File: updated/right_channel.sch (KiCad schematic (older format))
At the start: 20 parts, among them J4 Left 0 ohms, J5 Right 8 ohms, J6 Conn_Coaxial, T3 AudioTxfmr

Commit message: finish updated schematic
Convert tables from google doc to markdown to have these in this repo
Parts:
- removed RV1B: R_POT, symbol Device:R_POT
- removed V4,V5: 6P1, symbol local:6P1
- removed V7: 6H8C, symbol local:6H8C
- added RV1: R_POT_Dual_Separate, symbol Device:R_POT_Dual_Separate
- added V3: 12AX7, Valve:Valve_ECC-83-1, symbol local:12AX7
- added V4: EL84, Valve:Valve_ECC-83-1, symbol local:EL84
- C10, C11: footprint (none) -> Capacitor_THT:CP_Radial_D4.0mm_P2.00mm
- C12, C8: footprint (none) -> Capacitor_THT:CP_Radial_D10.0mm_P5.00mm
- C9: renamed from C12; footprint (none) -> Capacitor_THT:CP_Radial_D10.0mm_P5.00mm
- R10, R11, R7, R8, R9: footprint (none) -> Resistor_THT:R_Axial_DIN0516_L15.5mm_D5.0mm_P20.32mm_Horizontal
- R12: renamed from R?; footprint (none) -> Resistor_THT:R_Axial_DIN0516_L15.5mm_D5.0mm_P20.32mm_Horizontal
- R16: renamed from R16,17; footprint (none) -> Resistor_THT:R_Axial_DIN0516_L15.5mm_D5.0mm_P20.32mm_Horizontal
- R18: renamed from R13; footprint (none) -> Resistor_THT:R_Axial_DIN0516_L15.5mm_D5.0mm_P20.32mm_Horizontal
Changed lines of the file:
@@
 F 0 "C8" H 4318 1941 50  0000 L CNN
 F 1 "22uF" H 4318 1850 50  0000 L CNN
-F 2 "" H 4238 1700 50  0001 C CNN
+F 2 "Capacitor_THT:CP_Radial_D10.0mm_P5.00mm" H 4238 1700 50  0001 C CNN
 F 3 "~" H 4200 1850 50  0001 C CNN
 F 4 "450V" H 4318 1759 50  0000 L CNN "Voltage"
@@
 F 0 "R7" V 3643 1700 50  0000 C CNN
 F 1 "1.5K" V 3734 1700 50  0000 C CNN
-F 2 "" V 3780 1700 50  0001 C CNN
+F 2 "Resistor_THT:R_Axial_DIN0516_L15.5mm_D5.0mm_P20.32mm_Horizontal" V 3780 1700 50  0001 C CNN
 F 3 "~" H 3850 1700 50  0001 C CNN
 	1    3850 1700
@@
 AR Path="/5F20DF76" Ref="#PWR?"  Part="1"
 AR Path="/5F1F04D2/5F20DF76" Ref="#PWR?"  Part="1"
-AR Path="/5F200EB9/5F20DF76" Ref="#PWR?"  Part="1"
-F 0 "#PWR?" H 4200 1750 50  0001 C CNN
+AR Path="/5F200EB9/5F20DF76" Ref="#PWR09"  Part="1"
+F 0 "#PWR09" H 4200 1750 50  0001 C CNN
 F 1 "Earth" H 4200 1850 50  0001 C CNN
 F 2 "" H 4200 2000 50  0001 C CNN
@@
 F 0 "R9" H 4630 1804 50  0000 R CNN
 F 1 "30K" H 4630 1895 50  0000 R CNN
-F 2 "" V 4630 1850 50  0001 C CNN
+F 2 "Resistor_THT:R_Axial_DIN0516_L15.5mm_D5.0mm_P20.32mm_Horizontal" V 4630 1850 50  0001 C CNN
 F 3 "~" H 4700 1850 50  0001 C CNN
 	1    4700 1850
@@
 $EndComp
 Connection ~ 4200 1700
-$Comp
-L local:6H8C V?
-U 1 1 5F20DF83
-P 4700 2950
-AR Path="/5F20DF83" Ref="V?"  Part="1"
-AR Path="/5F1F04D2/5F20DF83" Ref="V?"  Part="1"
-AR Path="/5F200EB9/5F20DF83" Ref="V7"  Part="1"
-F 0 "V7" H 5008 2946 50  0000 L CNN
-F 1 "6H8C" H 5008 2855 50  0000 L CNN
-F 2 "" H 4720 2950 50  0001 C CNN
-F 3 "" H 4720 2950 50  0001 C CNN
-	1    4700 2950
-	1    0    0    -1
-$EndComp
 $Comp
 L Device:C C?
@@
 F 0 "C10" V 4798 2200 50  0000 C CNN
 F 1 "0.1uF" V 4900 2150 50  0000 C CNN
-F 2 "" H 5088 2050 50  0001 C CNN
+F 2 "Capacitor_THT:CP_Radial_D4.0mm_P2.00mm" H 5088 2050 50  0001 C CNN
 F 3 "~" H 5050 2200 50  0001 C CNN
 F 4 "450V" V 4900 2400 50  0000 C CNN "Voltage"
@@
 AR Path="/5F20DF90" Ref="R?"  Part="1"
 AR Path="/5F1F04D2/5F20DF90" Ref="R?"  Part="1"
-AR Path="/5F200EB9/5F20DF90" Ref="R?"  Part="1"
-F 0 "R?" V 4243 2400 50  0000 C CNN
+AR Path="/5F200EB9/5F20DF90" Ref="R12"  Part="1"
+F 0 "R12" V 4243 2400 50  0000 C CNN
 F 1 "470K" V 4334 2400 50  0000 C CNN
-F 2 "" V 4380 2400 50  0001 C CNN
+F 2 "Resistor_THT:R_Axial_DIN0516_L15.5mm_D5.0mm_P20.32mm_Horizontal" V 4380 2400 50  0001 C CNN
 F 3 "~" H 4450 2400 50  0001 C CNN
 	1    4450 2400
@@
 F 0 "C11" H 3750 2800 50  0000 L CNN
 F 1 "220K400" H 3750 2700 50  0000 L CNN
-F 2 "" H 4238 2600 50  0001 C CNN
+F 2 "Capacitor_THT:CP_Radial_D4.0mm_P2.00mm" H 4238 2600 50  0001 C CNN
 F 3 "~" H 4200 2750 50  0001 C CNN
 	1    4200 2750
@@
 AR Path="/5F20DF9D" Ref="R?"  Part="1"
 AR Path="/5F1F04D2/5F20DF9D" Ref="R?"  Part="1"
-AR Path="/5F200EB9/5F20DF9D" Ref="R13"  Part="1"
-F 0 "R13" H 4270 3296 50  0000 L CNN
+AR Path="/5F200EB9/5F20DF9D" Ref="R18"  Part="1"
+F 0 "R18" H 4270 3296 50  0000 L CNN
 F 1 "1M" H 4270 3205 50  0000 L CNN
-F 2 "" V 4130 3250 50  0001 C CNN
+F 2 "Resistor_THT:R_Axial_DIN0516_L15.5mm_D5.0mm_P20.32mm_Horizontal" V 4130 3250 50  0001 C CNN
 F 3 "~" H 4200 3250 50  0001 C CNN
 	1    4200 3250
 	1    0    0    -1
 $EndComp
-$Comp
-L local:6H8C V?
-U 2 1 5F20DFA3
-P 4700 4300
-AR Path="/5F20DFA3" Ref="V?"  Part="2"
-AR Path="/5F1F04D2/5F20DFA3" Ref="V?"  Part="2"
-AR Path="/5F200EB9/5F20DFA3" Ref="V7"  Part="2"
-F 0 "V7" H 5008 4296 50  0000 L CNN
-F 1 "6H8C" H 5008 4205 50  0000 L CNN
-F 2 "" H 4720 4300 50  0001 C CNN
-F 3 "" H 4720 4300 50  0001 C CNN
-	2    4700 4300
-	1    0    0    -1
-$EndComp
 Wire Wire Line
 	4200 3400 4200 3850
 Wire Wire Line
 	4950 3500 4950 3850
-Wire Wire Line
-	4700 3850 4950 3850
 $Comp
 L Connector:Conn_Coaxial J?
@@
 	-1   0    0    -1
 $EndComp
-$Comp
-L Device:R_POT RV1A?
-U 1 1 5F20DFB2
-P 3900 4350
-AR Path="/5F20DFB2" Ref="RV1A?"  Part="1"
-AR Path="/5F1F04D2/5F20DFB2" Ref="RV1A?"  Part="1"
-AR Path="/5F200EB9/5F20DFB2" Ref="RV1B"  Part="1"
-F 0 "RV1B" H 3831 4396 50  0000 R CNN
-F 1 "R_POT" H 3831 4305 50  0000 R CNN
-F 2 "" H 3900 4350 50  0001 C CNN
-F 3 "~" H 3900 4350 50  0001 C CNN
-	1    3900 4350
-	1    0    0    -1
-$EndComp
 Wire Wire Line
 	3900 4500 3900 5750
@@
 AR Path="/5F20DFBB" Ref="#PWR?"  Part="1"
 AR Path="/5F1F04D2/5F20DFBB" Ref="#PWR?"  Part="1"
-AR Path="/5F200EB9/5F20DFBB" Ref="#PWR?"  Part="1"
-F 0 "#PWR?" H 3350 5500 50  0001 C CNN
+AR Path="/5F200EB9/5F20DFBB" Ref="#PWR08"  Part="1"
+F 0 "#PWR08" H 3350 5500 50  0001 C CNN
 F 1 "Earth" H 3350 5600 50  0001 C CNN
 F 2 "" H 3350 5750 50  0001 C CNN
@@
 Wire Wire Line
 	4050 4350 4200 4350
-Text Label 4600 3550 2    50   ~ 0
+Text Label 4600 3500 2    50   ~ 0
 fl1
-Text Label 4800 3550 2    50   ~ 0
+Text Label 4800 3500 2    50   ~ 0
 fl2
 Text Label 4600 4850 2    50   ~ 0
@@
 F 0 "R10" H 4270 4746 50  0000 L CNN
 F 1 "470K" H 4270 4655 50  0000 L CNN
-F 2 "" V 4130 4700 50  0001 C CNN
+F 2 "Resistor_THT:R_Axial_DIN0516_L15.5mm_D5.0mm_P20.32mm_Horizontal" V 4130 4700 50  0001 C CNN
 F 3 "~" H 4200 4700 50  0001 C CNN
 	1    4200 4700
@@
 F 0 "R8" H 4820 5396 50  0000 L CNN
 F 1 "2.2K" H 4820 5305 50  0000 L CNN
-F 2 "" V 4680 5350 50  0001 C CNN
+F 2 "Resistor_THT:R_Axial_DIN0516_L15.5mm_D5.0mm_P20.32mm_Horizontal" V 4680 5350 50  0001 C CNN
 F 3 "~" H 4750 5350 50  0001 C CNN
 	1    4750 5350
@@
 AR Path="/5F20DFD9" Ref="C?"  Part="1"
 AR Path="/5F1F04D2/5F20DFD9" Ref="C?"  Part="1"
-AR Path="/5F200EB9/5F20DFD9" Ref="C12"  Part="1"
-F 0 "C12" H 5218 5441 50  0000 L CNN
+AR Path="/5F200EB9/5F20DFD9" Ref="C9"  Part="1"
+F 0 "C9" H 5218 5441 50  0000 L CNN
 F 1 "100uF" H 5218 5350 50  0000 L CNN
-F 2 "" H 5138 5200 50  0001 C CNN
+F 2 "Capacitor_THT:CP_Radial_D10.0mm_P5.00mm" H 5138 5200 50  0001 C CNN
 F 3 "~" H 5100 5350 50  0001 C CNN
 F 4 "25V" H 5218 5259 50  0000 L CNN "Voltage"
@@
 Wire Wire Line
 	4200 2900 4200 3000
-Wire Wire Line
-	4700 3850 4200 3850
-Connection ~ 4700 3850
 Wire Wire Line
 	4350 3000 4200 3000
@@
 Wire Wire Line
 	7650 1850 7550 1850
-$Comp
-L local:6P1 V2,V?
-U 1 1 5F20E00F
-P 6950 2950
-AR Path="/5F20E00F" Ref="V2,V?"  Part="1"
-AR Path="/5F1F04D2/5F20E00F" Ref="V2,V?"  Part="1"
-AR Path="/5F200EB9/5F20E00F" Ref="V4,V5"  Part="1"
-F 0 "V4,V5" H 7258 2946 50  0000 L CNN
-F 1 "6P1" H 7258 2855 50  0000 L CNN
-F 2 "" H 6970 2850 50  0001 C CNN
-F 3 "" H 6970 2850 50  0001 C CNN
-	1    6950 2950
-	1    0    0    -1
-$EndComp
 Wire Wire Line
 	6600 3150 5700 3150
@@
 AR Path="/5F20E019" Ref="R?"  Part="1"
 AR Path="/5F1F04D2/5F20E019" Ref="R?"  Part="1"
-AR Path="/5F200EB9/5F20E019" Ref="R16,17"  Part="1"
-F 0 "R16,17" H 6570 2846 50  0000 L CNN
+AR Path="/5F200EB9/5F20E019" Ref="R16"  Part="1"
+F 0 "R16" H 6570 2846 50  0000 L CNN
 F 1 "100" H 6570 2755 50  0000 L CNN
-F 2 "" V 6430 2800 50  0001 C CNN
+F 2 "Resistor_THT:R_Axial_DIN0516_L15.5mm_D5.0mm_P20.32mm_Horizontal" V 6430 2800 50  0001 C CNN
 F 3 "~" H 6500 2800 50  0001 C CNN
 	1    6500 2800
@@
 Wire Wire Line
 	6950 2150 6950 2500
-Connection ~ 6950 2500
 $Comp
 L Device:CP C?
@@
 F 0 "C12" H 7468 4041 50  0000 L CNN
 F 1 "220uF" H 7468 3950 50  0000 L CNN
-F 2 "" H 7388 3800 50  0001 C CNN
+F 2 "Capacitor_THT:CP_Radial_D10.0mm_P5.00mm" H 7388 3800 50  0001 C CNN
 F 3 "~" H 7350 3950 50  0001 C CNN
 F 4 "50V" H 7468 3859 50  0000 L CNN "Voltage"
@@
 F 0 "R11" H 7070 3996 50  0000 L CNN
 F 1 "270" H 7070 3905 50  0000 L CNN
-F 2 "" V 6930 3950 50  0001 C CNN
+F 2 "Resistor_THT:R_Axial_DIN0516_L15.5mm_D5.0mm_P20.32mm_Horizontal" V 6930 3950 50  0001 C CNN
 F 3 "~" H 7000 3950 50  0001 C CNN
 F 4 "5W" H 7000 3950 50  0001 C CNN "Power"
@@
 Wire Wire Line
 	3550 1700 3450 1700
+Wire Wire Line
+	4200 3850 4700 3850
+$Comp
+L local:EL84 V4
+U 1 1 5F223B2B
+P 6950 2950
+F 0 "V4" H 7258 2946 50  0000 L CNN
+F 1 "EL84" H 7258 2855 50  0000 L CNN
+F 2 "Valve:Valve_ECC-83-1" H 6970 2850 50  0001 C CNN
+F 3 "" H 6970 2850 50  0001 C CNN
+	1    6950 2950
+	1    0    0    -1
+$EndComp
+Connection ~ 6950 2500
+$Comp
+L local:12AX7 V3
+U 1 1 5F225712
+P 4700 2950
+F 0 "V3" H 5008 2946 50  0000 L CNN
+F 1 "12AX7" H 5008 2855 50  0000 L CNN
+F 2 "Valve:Valve_ECC-83-1" H 4720 2950 50  0001 C CNN
+F 3 "" H 4720 2950 50  0001 C CNN
+	1    4700 2950
+	1    0    0    -1
+$EndComp
+$Comp
+L local:12AX7 V3
+U 2 1 5F22A5F0
+P 4700 4300
+F 0 "V3" H 5008 4296 50  0000 L CNN
+F 1 "12AX7" H 5008 4205 50  0000 L CNN
+F 2 "Valve:Valve_ECC-83-1" H 4720 4300 50  0001 C CNN
+F 3 "" H 4720 4300 50  0001 C CNN
+	2    4700 4300
+	1    0    0    -1
+$EndComp
+Connection ~ 4700 3850
+Wire Wire Line
+	4700 3850 4950 3850
+$Comp
+L Device:R_POT_Dual_Separate RV1
+U 2 1 5F245DA2
+P 3900 4350
+F 0 "RV1" H 3830 4396 50  0000 R CNN
+F 1 "R_POT_Dual_Separate" H 3830 4305 50  0000 R CNN
+F 2 "" H 3900 4350 50  0001 C CNN
+F 3 "~" H 3900 4350 50  0001 C CNN
+	2    3900 4350
+	1    0    0    -1
+$EndComp
 $EndSCHEMATC

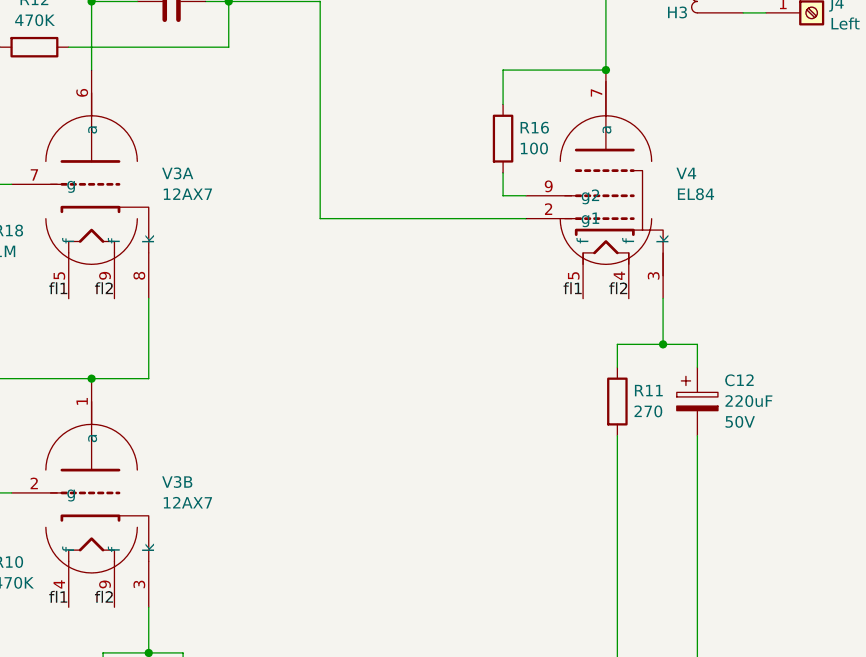
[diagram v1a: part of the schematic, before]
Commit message: add schematic for updated amp
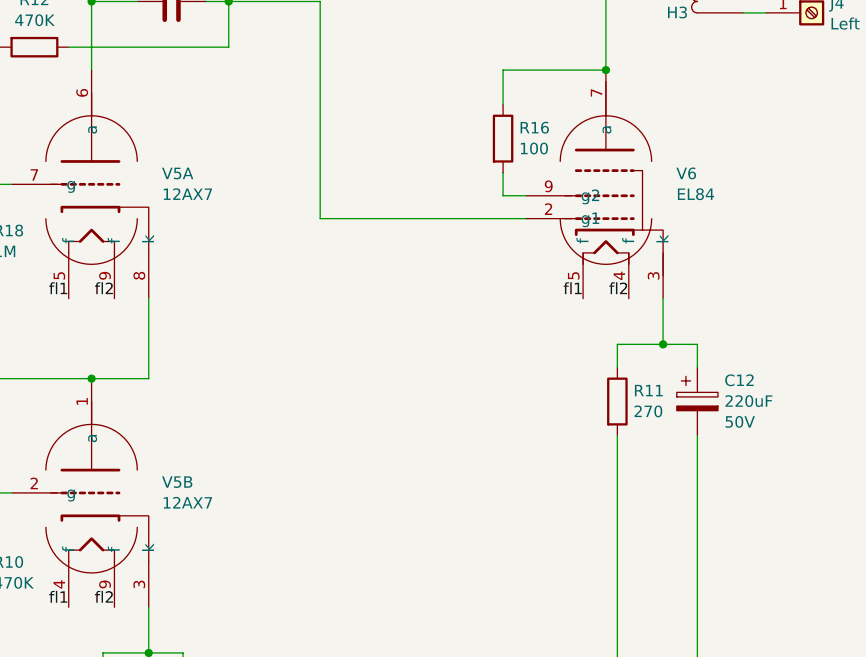
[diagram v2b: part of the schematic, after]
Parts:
- renumbered V3 to V5, V4 to V6
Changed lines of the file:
@@
 	4200 3850 4700 3850
 $Comp
-L local:EL84 V4
+L local:EL84 V6
 U 1 1 5F223B2B
 P 6950 2950
-F 0 "V4" H 7258 2946 50  0000 L CNN
+F 0 "V6" H 7258 2946 50  0000 L CNN
 F 1 "EL84" H 7258 2855 50  0000 L CNN
 F 2 "Valve:Valve_ECC-83-1" H 6970 2850 50  0001 C CNN
@@
 Connection ~ 6950 2500
 $Comp
-L local:12AX7 V3
+L local:12AX7 V5
 U 1 1 5F225712
 P 4700 2950
-F 0 "V3" H 5008 2946 50  0000 L CNN
+F 0 "V5" H 5008 2946 50  0000 L CNN
 F 1 "12AX7" H 5008 2855 50  0000 L CNN
 F 2 "Valve:Valve_ECC-83-1" H 4720 2950 50  0001 C CNN
@@
 $EndComp
 $Comp
-L local:12AX7 V3
+L local:12AX7 V5
 U 2 1 5F22A5F0
 P 4700 4300
-F 0 "V3" H 5008 4296 50  0000 L CNN
+F 0 "V5" H 5008 4296 50  0000 L CNN
 F 1 "12AX7" H 5008 4205 50  0000 L CNN
 F 2 "Valve:Valve_ECC-83-1" H 4720 4300 50  0001 C CNN

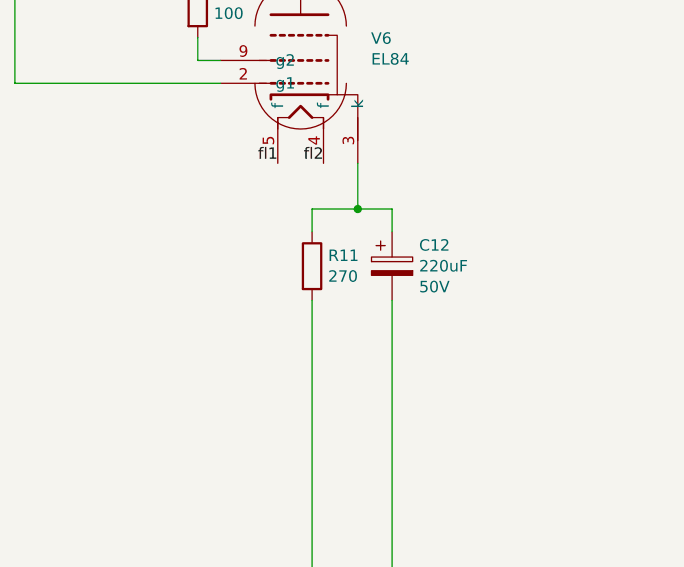
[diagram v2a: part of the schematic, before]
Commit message: install new electrolytic capacitors
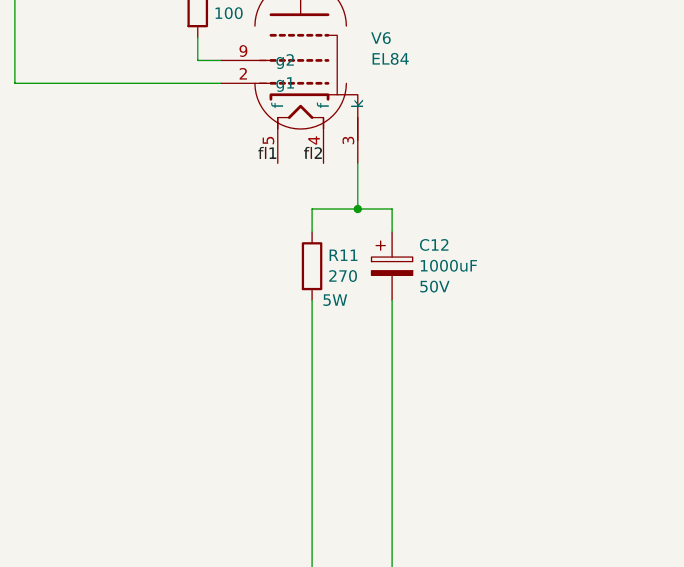
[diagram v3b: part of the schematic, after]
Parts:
- C12: value 220uF -> 1000uF
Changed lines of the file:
@@
 AR Path="/5F200EB9/5F20E026" Ref="C12"  Part="1"
 F 0 "C12" H 7468 4041 50  0000 L CNN
-F 1 "220uF" H 7468 3950 50  0000 L CNN
+F 1 "1000uF" H 7468 3950 50  0000 L CNN
 F 2 "Capacitor_THT:CP_Radial_D10.0mm_P5.00mm" H 7388 3800 50  0001 C CNN
 F 3 "~" H 7350 3950 50  0001 C CNN
@@
 	1    0    0    -1
 $EndComp
-$Comp
-L Device:R R?
-U 1 1 5F20E02D
-P 7000 3950
-AR Path="/5F20E02D" Ref="R?"  Part="1"
-AR Path="/5F1F04D2/5F20E02D" Ref="R?"  Part="1"
-AR Path="/5F200EB9/5F20E02D" Ref="R11"  Part="1"
-F 0 "R11" H 7070 3996 50  0000 L CNN
-F 1 "270" H 7070 3905 50  0000 L CNN
-F 2 "Resistor_THT:R_Axial_DIN0516_L15.5mm_D5.0mm_P20.32mm_Horizontal" V 6930 3950 50  0001 C CNN
-F 3 "~" H 7000 3950 50  0001 C CNN
-F 4 "5W" H 7000 3950 50  0001 C CNN "Power"
-	1    7000 3950
-	1    0    0    -1
-$EndComp
 Wire Wire Line
 	7200 3500 7200 3700
 Wire Wire Line
 	7200 3700 7000 3700
-Wire Wire Line
-	7000 3700 7000 3800
 Wire Wire Line
 	7200 3700 7350 3700
@@
 	1    0    0    -1
 $EndComp
+Wire Wire Line
+	7000 3700 7000 3800
+$Comp
+L Device:R R?
+U 1 1 5F20E02D
+P 7000 3950
+AR Path="/5F20E02D" Ref="R?"  Part="1"
+AR Path="/5F1F04D2/5F20E02D" Ref="R?"  Part="1"
+AR Path="/5F200EB9/5F20E02D" Ref="R11"  Part="1"
+F 0 "R11" H 7070 3996 50  0000 L CNN
+F 1 "270" H 7070 3905 50  0000 L CNN
+F 2 "Resistor_THT:R_Axial_DIN0516_L15.5mm_D5.0mm_P20.32mm_Horizontal" V 6930 3950 50  0001 C CNN
+F 3 "~" H 7000 3950 50  0001 C CNN
+F 4 "5W" H 7100 3800 50  0000 C CNN "Power"
+	1    7000 3950
+	1    0    0    -1
+$EndComp
